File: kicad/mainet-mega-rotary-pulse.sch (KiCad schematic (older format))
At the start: 0 parts

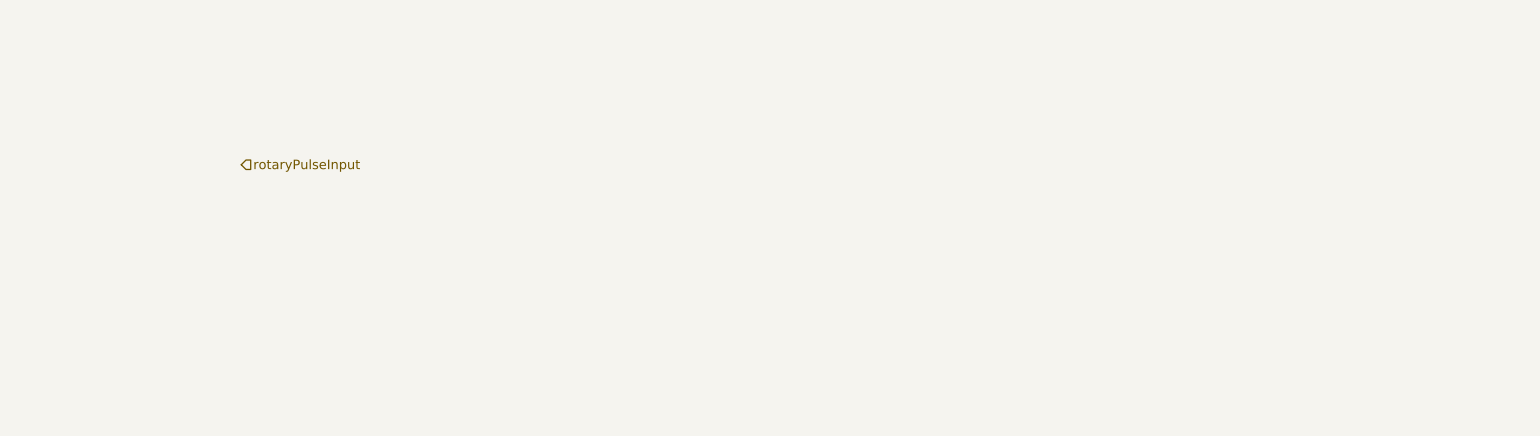
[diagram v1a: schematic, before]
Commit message: KiCAD: Se agregó el esquemático del circuito de traslación de voltaje del generador de pulsos de rotación
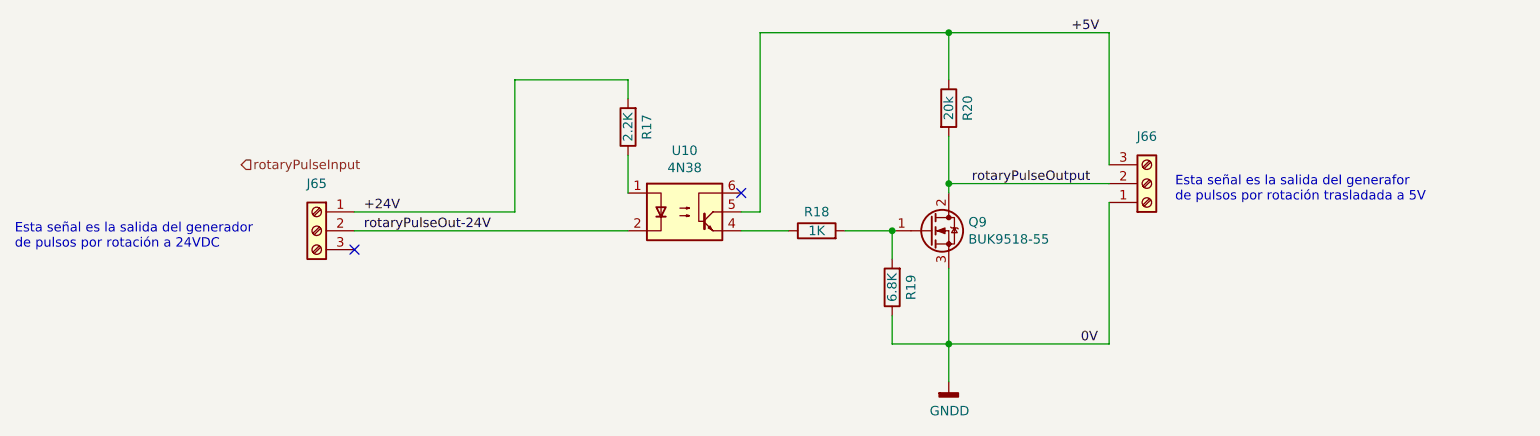
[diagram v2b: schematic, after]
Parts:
- added J65, J66: Screw_Terminal_01x03, TerminalBlock_Altech:Altech_AK300_1x03_P5.00mm_45-Degree, symbol Connector:Screw_Terminal_01x03
- added Q9: BUK9518-55, Package_TO_SOT_THT:TO-220-3_Vertical, symbol Transistor_FET:IRLZ44N
- added R17: 2.2K, Resistor_THT:R_Axial_DIN0207_L6.3mm_D2.5mm_P10.16mm_Horizontal, symbol Device:R
- added R18: 1K, Resistor_THT:R_Axial_DIN0207_L6.3mm_D2.5mm_P10.16mm_Horizontal, symbol Device:R
- added R19: 6.8K, Resistor_THT:R_Axial_DIN0207_L6.3mm_D2.5mm_P10.16mm_Horizontal, symbol Device:R
- added R20: 20k, Resistor_THT:R_Axial_DIN0207_L6.3mm_D2.5mm_P10.16mm_Horizontal, symbol Device:R
- added U10: 4N38, Package_DIP:DIP-6_W7.62mm, symbol Isolator:4N36
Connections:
- new net: Q9.1 (G), R18.2, R19.2
- new net: R17.1, U10.1
- new net: R18.1, U10.4
- new net +24V: J65.1 (Pin_1), R17.2
- new net +5V: J66.3 (Pin_3), R20.1, U10.5
- new net GNDD: J66.1 (Pin_1), Q9.3 (S), R19.1
- new net rotaryPulseOut-24V: J65.2 (Pin_2), U10.2
- new net rotaryPulseOutput: J66.2 (Pin_2), Q9.2 (D), R20.2
- no-connect marks 0 -> 2
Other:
- note added: "Esta señal es la salida del generador \nde pulsos por rotación a 24VDC\n"
- note added: "Esta señal es la salida del generafor\nde pulsos por rotación trasladada a 5V"
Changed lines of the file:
@@
 EESchema Schematic File Version 4
 LIBS:mainet-mega-cache
+LIBS:mainet-mega-rotary-pulse-generator-24v-to-mega-5v-cache
 EELAYER 30 0
 EELAYER END
 $Descr A4 11693 8268
 encoding utf-8
-Sheet 15 17
-Title ""
+Sheet 17 17
+Title "Rotary pulse traslator 24V to 5V"
 Date ""
 Rev ""
@@
 Text HLabel 2950 3500 2    50   Input ~ 0
 rotaryPulseInput
+$Comp
+L Transistor_FET:IRLZ44N Q?
+U 1 1 5F98737A
+P 6600 3850
+AR Path="/5F98737A" Ref="Q?"  Part="1"
+AR Path="/5F888A13/5F98737A" Ref="Q?"  Part="1"
+AR Path="/5F984CFE/5F98737A" Ref="Q?"  Part="1"
+AR Path="/5FC3A1C1/5F98737A" Ref="Q9"  Part="1"
+F 0 "Q9" H 6804 3896 50  0000 L CNN
+F 1 "BUK9518-55" H 6804 3805 50  0000 L CNN
+F 2 "Package_TO_SOT_THT:TO-220-3_Vertical" H 6850 3775 50  0001 L CIN
+F 3 "http://www.irf.com/product-info/datasheets/data/irlz44n.pdf" H 6600 3850 50  0001 L CNN
+	1    6600 3850
+	1    0    0    -1
+$EndComp
+$Comp
+L Isolator:4N36 U?
+U 1 1 5F987380
+P 5300 3750
+AR Path="/5F987380" Ref="U?"  Part="1"
+AR Path="/5F888A13/5F987380" Ref="U?"  Part="1"
+AR Path="/5F984CFE/5F987380" Ref="U?"  Part="1"
+AR Path="/5FC3A1C1/5F987380" Ref="U10"  Part="1"
+F 0 "U10" H 5300 4075 50  0000 C CNN
+F 1 "4N38" H 5300 3984 50  0000 C CNN
+F 2 "Package_DIP:DIP-6_W7.62mm" H 5100 3550 50  0001 L CIN
+F 3 "https://www.vishay.com/docs/81181/4n35.pdf" H 5300 3750 50  0001 L CNN
+	1    5300 3750
+	1    0    0    -1
+$EndComp
+$Comp
+L Device:R R?
+U 1 1 5F987386
+P 6400 4150
+AR Path="/5F987386" Ref="R?"  Part="1"
+AR Path="/5F888A13/5F987386" Ref="R?"  Part="1"
+AR Path="/5F984CFE/5F987386" Ref="R?"  Part="1"
+AR Path="/5FC3A1C1/5F987386" Ref="R19"  Part="1"
+F 0 "R19" V 6300 4150 50  0000 C CNN
+F 1 "6.8K" V 6400 4150 50  0000 C CNN
+F 2 "Resistor_THT:R_Axial_DIN0207_L6.3mm_D2.5mm_P10.16mm_Horizontal" V 6330 4150 50  0001 C CNN
+F 3 "~" H 6400 4150 50  0001 C CNN
+	1    6400 4150
+	-1   0    0    1
+$EndComp
+Wire Wire Line
+	6400 3850 6400 4000
+$Comp
+L Device:R R?
+U 1 1 5F987394
+P 6000 3850
+AR Path="/5F987394" Ref="R?"  Part="1"
+AR Path="/5F888A13/5F987394" Ref="R?"  Part="1"
+AR Path="/5F984CFE/5F987394" Ref="R?"  Part="1"
+AR Path="/5FC3A1C1/5F987394" Ref="R18"  Part="1"
+F 0 "R18" V 6100 3850 50  0000 C CNN
+F 1 "1K" V 6000 3850 50  0000 C CNN
+F 2 "Resistor_THT:R_Axial_DIN0207_L6.3mm_D2.5mm_P10.16mm_Horizontal" V 5930 3850 50  0001 C CNN
+F 3 "~" H 6000 3850 50  0001 C CNN
+	1    6000 3850
+	0    -1   -1   0
+$EndComp
+Connection ~ 6400 3850
+Wire Wire Line
+	6150 3850 6400 3850
+Wire Wire Line
+	5700 3750 5600 3750
+$Comp
+L Device:R R?
+U 1 1 5F9873B0
+P 5000 3300
+AR Path="/5F9873B0" Ref="R?"  Part="1"
+AR Path="/5F888A13/5F9873B0" Ref="R?"  Part="1"
+AR Path="/5F984CFE/5F9873B0" Ref="R?"  Part="1"
+AR Path="/5FC3A1C1/5F9873B0" Ref="R17"  Part="1"
+F 0 "R17" V 4900 3300 50  0000 C CNN
+F 1 "2.2K" V 5000 3300 50  0000 C CNN
+F 2 "Resistor_THT:R_Axial_DIN0207_L6.3mm_D2.5mm_P10.16mm_Horizontal" V 4930 3300 50  0001 C CNN
+F 3 "~" H 5000 3300 50  0001 C CNN
+	1    5000 3300
+	-1   0    0    1
+$EndComp
+Wire Wire Line
+	5000 3450 5000 3650
+Wire Wire Line
+	4400 3050 5000 3050
+Wire Wire Line
+	5000 3050 5000 3150
+Wire Wire Line
+	4400 3050 4400 3750
+$Comp
+L Connector:Screw_Terminal_01x03 J?
+U 1 1 5F9873C9
+P 7750 3600
+AR Path="/5F9873C9" Ref="J?"  Part="1"
+AR Path="/5F888A13/5F9873C9" Ref="J?"  Part="1"
+AR Path="/5F984CFE/5F9873C9" Ref="J?"  Part="1"
+AR Path="/5FC3A1C1/5F9873C9" Ref="J66"  Part="1"
+F 0 "J66" H 7750 3350 50  0000 C CNN
+F 1 "Screw_Terminal_01x03" H 7668 3366 50  0001 C CNN
+F 2 "TerminalBlock_Altech:Altech_AK300_1x03_P5.00mm_45-Degree" H 7750 3600 50  0001 C CNN
+F 3 "~" H 7750 3600 50  0001 C CNN
+	1    7750 3600
+	1    0    0    1
+$EndComp
+NoConn ~ 5600 3650
+Wire Wire Line
+	7550 3600 6700 3600
+Wire Wire Line
+	6700 3600 6700 3650
+Wire Wire Line
+	6700 2800 7550 2800
+Wire Wire Line
+	7550 2800 7550 3500
+Connection ~ 6700 2800
+Wire Wire Line
+	5700 2800 6700 2800
+$Comp
+L Device:R R?
+U 1 1 5F9873EB
+P 6700 3200
+AR Path="/5F9873EB" Ref="R?"  Part="1"
+AR Path="/5F888A13/5F9873EB" Ref="R?"  Part="1"
+AR Path="/5F984CFE/5F9873EB" Ref="R?"  Part="1"
+AR Path="/5FC3A1C1/5F9873EB" Ref="R20"  Part="1"
+F 0 "R20" V 6800 3200 50  0000 C CNN
+F 1 "20k" V 6700 3200 50  0000 C CNN
+F 2 "Resistor_THT:R_Axial_DIN0207_L6.3mm_D2.5mm_P10.16mm_Horizontal" V 6630 3200 50  0001 C CNN
+F 3 "~" H 6700 3200 50  0001 C CNN
+	1    6700 3200
+	1    0    0    -1
+$EndComp
+Wire Wire Line
+	6700 2800 6700 3050
+Wire Wire Line
+	6700 3350 6700 3600
+Connection ~ 6700 3600
+Wire Wire Line
+	3550 3750 4400 3750
+Wire Wire Line
+	5600 3850 5850 3850
+Wire Wire Line
+	5700 2800 5700 3750
+Text Label 3600 3850 0    50   ~ 0
+rotaryPulseOut-24V
+$Comp
+L Connector:Screw_Terminal_01x03 J?
+U 1 1 5FABEB04
+P 3350 3850
+AR Path="/5FABEB04" Ref="J?"  Part="1"
+AR Path="/5F888A13/5FABEB04" Ref="J?"  Part="1"
+AR Path="/5F984CFE/5FABEB04" Ref="J?"  Part="1"
+AR Path="/5FC3A1C1/5FABEB04" Ref="J65"  Part="1"
+F 0 "J65" H 3350 4100 50  0000 C CNN
+F 1 "Screw_Terminal_01x03" H 3268 3616 50  0001 C CNN
+F 2 "TerminalBlock_Altech:Altech_AK300_1x03_P5.00mm_45-Degree" H 3350 3850 50  0001 C CNN
+F 3 "~" H 3350 3850 50  0001 C CNN
+	1    3350 3850
+	-1   0    0    -1
+$EndComp
+Wire Wire Line
+	3550 3850 5000 3850
+Text Label 3600 3750 0    50   ~ 0
++24V
+Text Label 7350 2800 0    50   ~ 0
++5V
+Wire Wire Line
+	6400 4300 6400 4450
+Wire Wire Line
+	6400 4450 6700 4450
+Wire Wire Line
+	7550 4450 7550 3700
+Wire Wire Line
+	6700 4050 6700 4450
+Connection ~ 6700 4450
+Wire Wire Line
+	6700 4450 7550 4450
+Text Label 7450 3600 2    50   ~ 0
+rotaryPulseOutput
+Text Label 7400 4450 0    50   ~ 0
+0V
+NoConn ~ 3550 3950
+Text Notes 1750 3950 0    50   ~ 0
+Esta señal es la salida del generador \nde pulsos por rotación a 24VDC\n
+Text Notes 7900 3700 0    50   ~ 0
+Esta señal es la salida del generafor\nde pulsos por rotación trasladada a 5V
+$Comp
+L power:GNDD #PWR040
+U 1 1 601BAD38
+P 6700 4650
+F 0 "#PWR040" H 6700 4400 50  0001 C CNN
+F 1 "GNDD" H 6704 4495 50  0000 C CNN
+F 2 "" H 6700 4650 50  0001 C CNN
+F 3 "" H 6700 4650 50  0001 C CNN
+	1    6700 4650
+	1    0    0    -1
+$EndComp
+Wire Wire Line
+	6700 4450 6700 4650
 $EndSCHEMATC

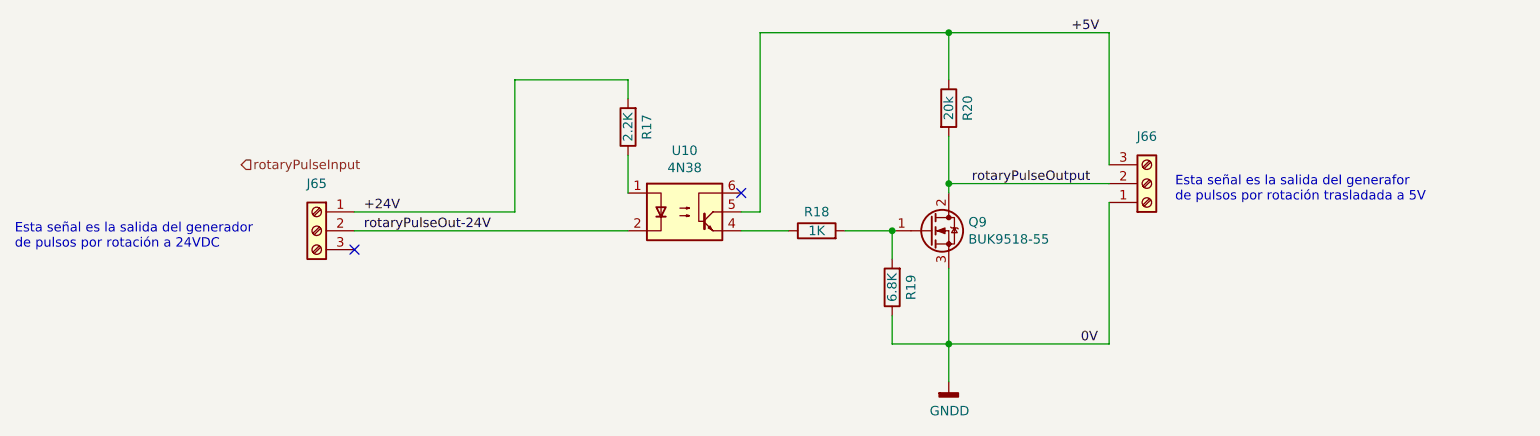
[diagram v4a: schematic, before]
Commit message: KICAD: Modificar mainet-mega-rotary-pulse.sch
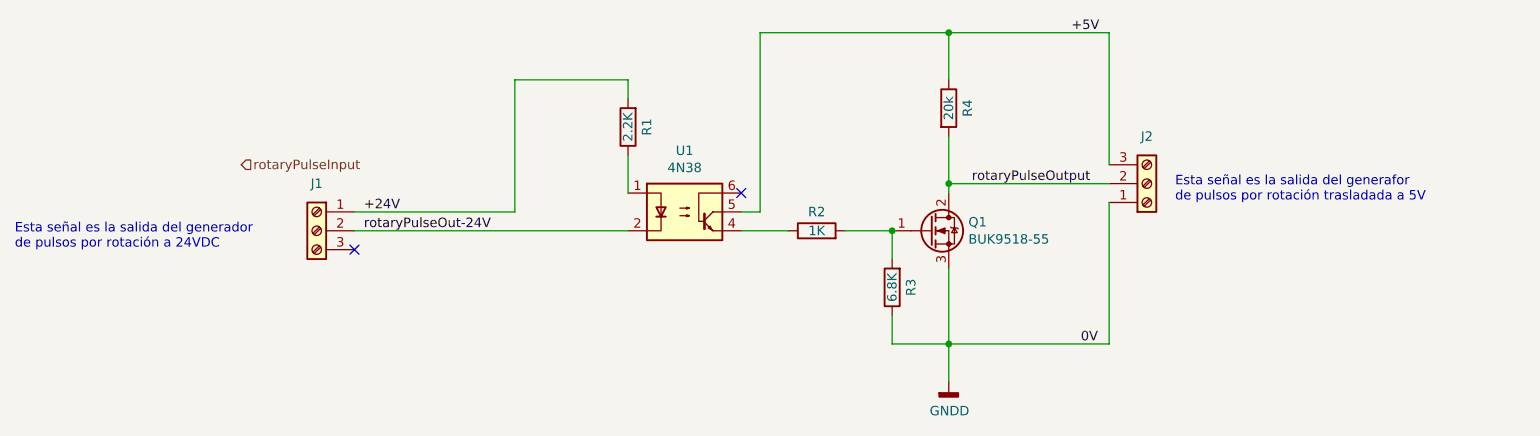
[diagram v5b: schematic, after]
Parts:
- R1: renamed from R17; footprint Resistor_THT:R_Axial_DIN0207_L6.3mm_D2.5mm_P10.16mm_Horizontal -> Resistor_THT:R_Axial_DIN0414_L11.9mm_D4.5mm_P15.24mm_Horizontal
- R2: renamed from R18; footprint Resistor_THT:R_Axial_DIN0207_L6.3mm_D2.5mm_P10.16mm_Horizontal -> Resistor_THT:R_Axial_DIN0414_L11.9mm_D4.5mm_P15.24mm_Horizontal
- R3: renamed from R19; footprint Resistor_THT:R_Axial_DIN0207_L6.3mm_D2.5mm_P10.16mm_Horizontal -> Resistor_THT:R_Axial_DIN0414_L11.9mm_D4.5mm_P15.24mm_Horizontal
- renumbered J65 to J1, J66 to J2, Q9 to Q1, R20 to R4, U10 to U1
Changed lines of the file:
@@
 EESchema Schematic File Version 4
-LIBS:mainet-mega-cache
+LIBS:mainet-mega-rotary-pulse-cache
 EELAYER 30 0
 EELAYER END
 $Descr A4 11693 8268
 encoding utf-8
-Sheet 17 21
+Sheet 1 1
 Title "Rotary pulse traslator 24V to 5V"
 Date ""
@@
 rotaryPulseInput
 $Comp
-L Transistor_FET:IRLZ44N Q?
+L Transistor_FET:IRLZ44N Q1
 U 1 1 5F98737A
 P 6600 3850
-AR Path="/5F98737A" Ref="Q?"  Part="1"
+AR Path="/5F98737A" Ref="Q1"  Part="1"
 AR Path="/5F888A13/5F98737A" Ref="Q?"  Part="1"
 AR Path="/5F984CFE/5F98737A" Ref="Q?"  Part="1"
 AR Path="/5FC3A1C1/5F98737A" Ref="Q9"  Part="1"
-F 0 "Q9" H 6804 3896 50  0000 L CNN
+F 0 "Q1" H 6804 3896 50  0000 L CNN
 F 1 "BUK9518-55" H 6804 3805 50  0000 L CNN
 F 2 "Package_TO_SOT_THT:TO-220-3_Vertical" H 6850 3775 50  0001 L CIN
@@
 $EndComp
 $Comp
-L Isolator:4N36 U?
+L Isolator:4N36 U1
 U 1 1 5F987380
 P 5300 3750
-AR Path="/5F987380" Ref="U?"  Part="1"
+AR Path="/5F987380" Ref="U1"  Part="1"
 AR Path="/5F888A13/5F987380" Ref="U?"  Part="1"
 AR Path="/5F984CFE/5F987380" Ref="U?"  Part="1"
 AR Path="/5FC3A1C1/5F987380" Ref="U10"  Part="1"
-F 0 "U10" H 5300 4075 50  0000 C CNN
+F 0 "U1" H 5300 4075 50  0000 C CNN
 F 1 "4N38" H 5300 3984 50  0000 C CNN
 F 2 "Package_DIP:DIP-6_W7.62mm" H 5100 3550 50  0001 L CIN
@@
 $EndComp
 $Comp
-L Device:R R?
+L Device:R R3
 U 1 1 5F987386
 P 6400 4150
-AR Path="/5F987386" Ref="R?"  Part="1"
+AR Path="/5F987386" Ref="R3"  Part="1"
 AR Path="/5F888A13/5F987386" Ref="R?"  Part="1"
 AR Path="/5F984CFE/5F987386" Ref="R?"  Part="1"
 AR Path="/5FC3A1C1/5F987386" Ref="R19"  Part="1"
-F 0 "R19" V 6300 4150 50  0000 C CNN
+F 0 "R3" V 6300 4150 50  0000 C CNN
 F 1 "6.8K" V 6400 4150 50  0000 C CNN
-F 2 "Resistor_THT:R_Axial_DIN0207_L6.3mm_D2.5mm_P10.16mm_Horizontal" V 6330 4150 50  0001 C CNN
+F 2 "Resistor_THT:R_Axial_DIN0414_L11.9mm_D4.5mm_P15.24mm_Horizontal" V 6330 4150 50  0001 C CNN
 F 3 "~" H 6400 4150 50  0001 C CNN
 	1    6400 4150
@@
 	6400 3850 6400 4000
 $Comp
-L Device:R R?
+L Device:R R2
 U 1 1 5F987394
 P 6000 3850
-AR Path="/5F987394" Ref="R?"  Part="1"
+AR Path="/5F987394" Ref="R2"  Part="1"
 AR Path="/5F888A13/5F987394" Ref="R?"  Part="1"
 AR Path="/5F984CFE/5F987394" Ref="R?"  Part="1"
 AR Path="/5FC3A1C1/5F987394" Ref="R18"  Part="1"
-F 0 "R18" V 6100 3850 50  0000 C CNN
+F 0 "R2" V 6100 3850 50  0000 C CNN
 F 1 "1K" V 6000 3850 50  0000 C CNN
-F 2 "Resistor_THT:R_Axial_DIN0207_L6.3mm_D2.5mm_P10.16mm_Horizontal" V 5930 3850 50  0001 C CNN
+F 2 "Resistor_THT:R_Axial_DIN0414_L11.9mm_D4.5mm_P15.24mm_Horizontal" V 5930 3850 50  0001 C CNN
 F 3 "~" H 6000 3850 50  0001 C CNN
 	1    6000 3850
@@
 	5700 3750 5600 3750
 $Comp
-L Device:R R?
+L Device:R R1
 U 1 1 5F9873B0
 P 5000 3300
-AR Path="/5F9873B0" Ref="R?"  Part="1"
+AR Path="/5F9873B0" Ref="R1"  Part="1"
 AR Path="/5F888A13/5F9873B0" Ref="R?"  Part="1"
 AR Path="/5F984CFE/5F9873B0" Ref="R?"  Part="1"
 AR Path="/5FC3A1C1/5F9873B0" Ref="R17"  Part="1"
-F 0 "R17" V 4900 3300 50  0000 C CNN
+F 0 "R1" V 4900 3300 50  0000 C CNN
 F 1 "2.2K" V 5000 3300 50  0000 C CNN
-F 2 "Resistor_THT:R_Axial_DIN0207_L6.3mm_D2.5mm_P10.16mm_Horizontal" V 4930 3300 50  0001 C CNN
+F 2 "Resistor_THT:R_Axial_DIN0414_L11.9mm_D4.5mm_P15.24mm_Horizontal" V 4930 3300 50  0001 C CNN
 F 3 "~" H 5000 3300 50  0001 C CNN
 	1    5000 3300
@@
 	4400 3050 4400 3750
 $Comp
-L Connector:Screw_Terminal_01x03 J?
+L Connector:Screw_Terminal_01x03 J2
 U 1 1 5F9873C9
 P 7750 3600
-AR Path="/5F9873C9" Ref="J?"  Part="1"
+AR Path="/5F9873C9" Ref="J2"  Part="1"
 AR Path="/5F888A13/5F9873C9" Ref="J?"  Part="1"
 AR Path="/5F984CFE/5F9873C9" Ref="J?"  Part="1"
 AR Path="/5FC3A1C1/5F9873C9" Ref="J66"  Part="1"
-F 0 "J66" H 7750 3350 50  0000 C CNN
+F 0 "J2" H 7750 3350 50  0000 C CNN
 F 1 "Screw_Terminal_01x03" H 7668 3366 50  0001 C CNN
 F 2 "TerminalBlock_Altech:Altech_AK300_1x03_P5.00mm_45-Degree" H 7750 3600 50  0001 C CNN
@@
 	5700 2800 6700 2800
 $Comp
-L Device:R R?
+L Device:R R4
 U 1 1 5F9873EB
 P 6700 3200
-AR Path="/5F9873EB" Ref="R?"  Part="1"
+AR Path="/5F9873EB" Ref="R4"  Part="1"
 AR Path="/5F888A13/5F9873EB" Ref="R?"  Part="1"
 AR Path="/5F984CFE/5F9873EB" Ref="R?"  Part="1"
 AR Path="/5FC3A1C1/5F9873EB" Ref="R20"  Part="1"
-F 0 "R20" V 6800 3200 50  0000 C CNN
+F 0 "R4" V 6800 3200 50  0000 C CNN
 F 1 "20k" V 6700 3200 50  0000 C CNN
 F 2 "Resistor_THT:R_Axial_DIN0207_L6.3mm_D2.5mm_P10.16mm_Horizontal" V 6630 3200 50  0001 C CNN
@@
 rotaryPulseOut-24V
 $Comp
-L Connector:Screw_Terminal_01x03 J?
+L Connector:Screw_Terminal_01x03 J1
 U 1 1 5FABEB04
 P 3350 3850
-AR Path="/5FABEB04" Ref="J?"  Part="1"
+AR Path="/5FABEB04" Ref="J1"  Part="1"
 AR Path="/5F888A13/5FABEB04" Ref="J?"  Part="1"
 AR Path="/5F984CFE/5FABEB04" Ref="J?"  Part="1"
 AR Path="/5FC3A1C1/5FABEB04" Ref="J65"  Part="1"
-F 0 "J65" H 3350 4100 50  0000 C CNN
+F 0 "J1" H 3350 4100 50  0000 C CNN
 F 1 "Screw_Terminal_01x03" H 3268 3616 50  0001 C CNN
 F 2 "TerminalBlock_Altech:Altech_AK300_1x03_P5.00mm_45-Degree" H 3350 3850 50  0001 C CNN
